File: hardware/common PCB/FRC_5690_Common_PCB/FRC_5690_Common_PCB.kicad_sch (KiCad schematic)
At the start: 33 parts, among them J1 5V in, J10 UART, J11 LED 0, J12 LED 1, J13 Analog In, J17 Conn_01x03_Pin, J18 Conn_01x03_Pin, J19 Conn_01x03_Pin, J2 I2C 0, J20 Conn_01x03_Pin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

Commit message: migrate to Pico code and add micro SD card slot
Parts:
- added C3: 100nF, Capacitor_SMD:C_0603_1608Metric, symbol Device:C
- added J14: Micro_SD_Card, Connector_Card:microSD_HC_Hirose_DM3BT-DSF-PEJS, symbol Connector:Micro_SD_Card
- added R5: 1k, Resistor_SMD:R_0603_1608Metric, symbol Device:R
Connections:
- net +3.3V: now also C3.1, J14.4 (VDD), R5.1
- net GND: now also C3.2, J14.6 (VSS), J14.9 (SHIELD)
- net SPI1_CLK: now also J14.5 (CLK)
- net SPI1_MISO: now also J14.7 (DAT0)
- net SPI1_MOSI: now also J14.3 (CMD)
- net SD_CARD_CS: now reaches U1.29 (GPIO22)
- net SD_CARD_CS: now also J14.2 (DAT3/CD), R5.2
- no-connect marks 0 -> 2

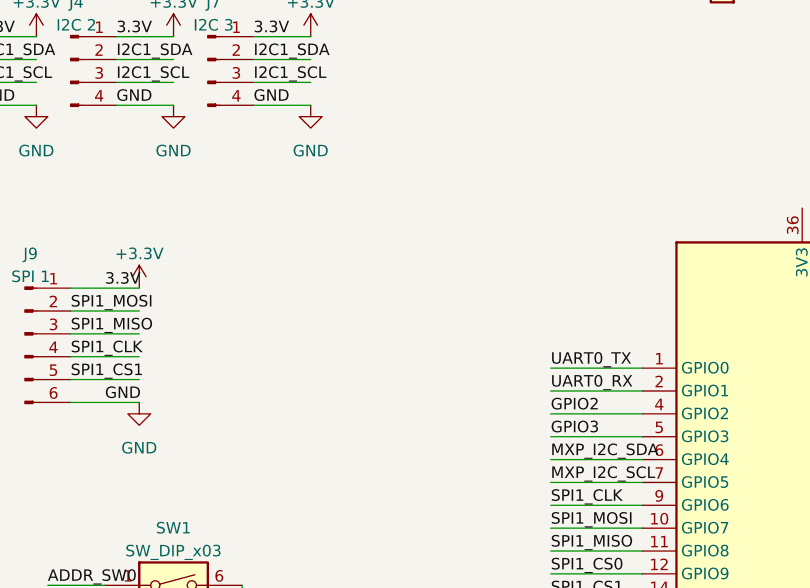
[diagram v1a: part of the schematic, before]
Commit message: Add EEPROM
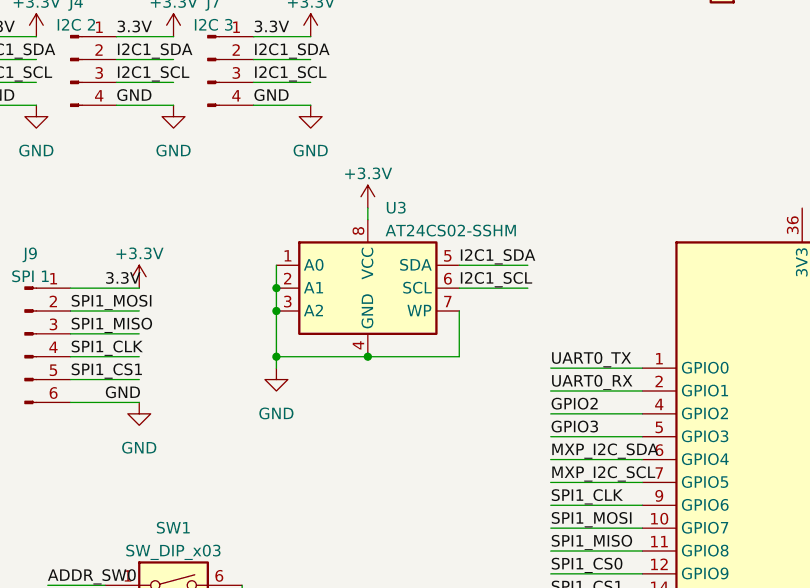
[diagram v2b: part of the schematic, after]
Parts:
- added U3: AT24CS02-SSHM, Package_SO:SOIC-8_3.9x4.9mm_P1.27mm, symbol Memory_EEPROM:AT24CS02-SSHM
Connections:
- net +3.3V: now also U3.8 (VCC)
- net GND: now also U3.1 (A0), U3.2 (A1), U3.3 (A2), U3.4 (GND), U3.7 (WP)
- net I2C1_SCL: now also U3.6 (SCL)
- net I2C1_SDA: now also U3.5 (SDA)
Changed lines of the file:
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@@
     (comment 1 "Designed by Evan Rust")
   )
+  (junction (at 88.9 73.66) (diameter 0) (color 0 0 0 0)
+  )
   (junction (at 222.25 149.86) (diameter 0) (color 0 0 0 0)
   )
@@
   (junction (at 232.41 49.53) (diameter 0) (color 0 0 0 0)
   )
+  (junction (at 99.06 73.66) (diameter 0) (color 0 0 0 0)
+  )
+  (junction (at 88.9 66.04) (diameter 0) (color 0 0 0 0)
+  )
   (junction (at 222.25 133.35) (diameter 0) (color 0 0 0 0)
   )
   (junction (at 232.41 93.98) (diameter 0) (color 0 0 0 0)
   )
+  (junction (at 88.9 68.58) (diameter 0) (color 0 0 0 0)
+  )
   (junction (at 224.79 63.5) (diameter 0) (color 0 0 0 0)
   )
@@
     (stroke (width 0) (type default))
   )
+  (wire (pts (xy 109.22 68.58) (xy 109.22 73.66))
+    (stroke (width 0) (type default))
+  )
   (wire (pts (xy 36.83 152.4) (xy 46.99 152.4))
     (stroke (width 0) (type default))
@@
     (stroke (width 0) (type default))
   )
+  (wire (pts (xy 99.06 57.15) (xy 99.06 58.42))
+    (stroke (width 0) (type default))
+  )
   (wire (pts (xy 116.84 182.88) (xy 125.73 182.88))
     (stroke (width 0) (type default))
@@
     (stroke (width 0) (type default))
   )
+  (wire (pts (xy 99.06 73.66) (xy 88.9 73.66))
+    (stroke (width 0) (type default))
+  )
+  (wire (pts (xy 88.9 66.04) (xy 88.9 68.58))
+    (stroke (width 0) (type default))
+  )
   (wire (pts (xy 119.38 102.87) (xy 129.54 102.87))
     (stroke (width 0) (type default))
@@
     (stroke (width 0) (type default))
   )
+  (wire (pts (xy 88.9 68.58) (xy 88.9 73.66))
+    (stroke (width 0) (type default))
+  )
   (wire (pts (xy 189.23 146.05) (xy 194.31 146.05))
     (stroke (width 0) (type default))
@@
     (stroke (width 0) (type default))
   )
+  (wire (pts (xy 99.06 73.66) (xy 109.22 73.66))
+    (stroke (width 0) (type default))
+  )
   (wire (pts (xy 232.41 118.11) (xy 232.41 119.38))
     (stroke (width 0) (type default))
@@
     (stroke (width 0) (type default))
   )
+  (wire (pts (xy 88.9 73.66) (xy 88.9 74.93))
+    (stroke (width 0) (type default))
+  )
   (wire (pts (xy 119.38 90.17) (xy 129.54 90.17))
     (stroke (width 0) (type default))
@@
     (stroke (width 0) (type default))
   )
+  (wire (pts (xy 88.9 63.5) (xy 88.9 66.04))
+    (stroke (width 0) (type default))
+  )
   (wire (pts (xy 91.44 144.78) (xy 104.14 144.78))
     (stroke (width 0) (type default))
@@
     (stroke (width 0) (type default))
   )
+  (wire (pts (xy 109.22 63.5) (xy 116.84 63.5))
+    (stroke (width 0) (type default))
+  )
   (wire (pts (xy 119.38 85.09) (xy 129.54 85.09))
     (stroke (width 0) (type default))
   )
+  (wire (pts (xy 109.22 66.04) (xy 116.84 66.04))
+    (stroke (width 0) (type default))
+  )
   (wire (pts (xy 66.04 76.2) (xy 73.66 76.2))
     (stroke (width 0) (type default))
@@
     (effects (font (size 1.27 1.27)) (justify left bottom))
   )
+  (label "I2C1_SDA" (at 109.22 63.5 0) (fields_autoplaced)
+    (effects (font (size 1.27 1.27)) (justify left bottom))
+  )
   (label "SPI1_MISO" (at 41.91 71.12 0) (fields_autoplaced)
     (effects (font (size 1.27 1.27)) (justify left bottom))
@@
     (effects (font (size 1.27 1.27)) (justify left bottom))
   )
+  (label "I2C1_SCL" (at 109.22 66.04 0) (fields_autoplaced)
+    (effects (font (size 1.27 1.27)) (justify left bottom))
+  )
   (label "GPIO3" (at 189.23 135.89 0) (fields_autoplaced)
     (effects (font (size 1.27 1.27)) (justify left bottom))
@@
     )
   )
+  (symbol (lib_id "power:GND") (at 88.9 74.93 0) (unit 1)
+    (in_bom yes) (on_board yes) (dnp no) (fields_autoplaced)
+    (property "Reference" "#PWR060" (at 88.9 81.28 0)
+      (effects (font (size 1.27 1.27)) hide)
+    )
+    (property "Value" "GND" (at 88.9 80.01 0)
+      (effects (font (size 1.27 1.27)))
+    )
+    (property "Footprint" "" (at 88.9 74.93 0)
+      (effects (font (size 1.27 1.27)) hide)
+    )
+    (property "Datasheet" "" (at 88.9 74.93 0)
+      (effects (font (size 1.27 1.27)) hide)
+    )
+    (pin "1")
+    (instances
+      (project "FRC_5690_Common_PCB"
+        (path "/61912a13-ede8-48b1-a32d-9390036060d9"
+          (reference "#PWR060") (unit 1)
+        )
+      )
+    )
+  )
   (symbol (lib_id "Transistor_BJT:BC849W") (at 215.9 113.03 0) (unit 1)
     (in_bom yes) (on_board yes) (dnp no) (fields_autoplaced)
@@
     )
   )
+  (symbol (lib_id "power:+3.3V") (at 99.06 57.15 0) (unit 1)
+    (in_bom yes) (on_board yes) (dnp no) (fields_autoplaced)
+    (property "Reference" "#PWR059" (at 99.06 60.96 0)
+      (effects (font (size 1.27 1.27)) hide)
+    )
+    (property "Value" "+3.3V" (at 99.06 53.34 0)
+      (effects (font (size 1.27 1.27)))
+    )
+    (property "Footprint" "" (at 99.06 57.15 0)
+      (effects (font (size 1.27 1.27)) hide)
+    )
+    (property "Datasheet" "" (at 99.06 57.15 0)
+      (effects (font (size 1.27 1.27)) hide)
+    )
+    (pin "1")
+    (instances
+      (project "FRC_5690_Common_PCB"
+        (path "/61912a13-ede8-48b1-a32d-9390036060d9"
+          (reference "#PWR059") (unit 1)
+        )
+      )
+    )
+  )
   (symbol (lib_id "Connector:Screw_Terminal_01x02") (at 138.43 33.02 180) (unit 1)
     (in_bom yes) (on_board yes) (dnp no) (fields_autoplaced)
@@
         )
       )
+    )
+  )
+  (symbol (lib_id "Memory_EEPROM:AT24CS02-SSHM") (at 99.06 66.04 0) (unit 1)
+    (in_bom yes) (on_board yes) (dnp no) (fields_autoplaced)
+    (property "Reference" "U3" (at 101.0159 57.15 0)
+      (effects (font (size 1.27 1.27)) (justify left))
+    )
+    (property "Value" "AT24CS02-SSHM" (at 101.0159 59.69 0)
+      (effects (font (size 1.27 1.27)) (justify left))
+    )
+    (property "Footprint" "Package_SO:SOIC-8_3.9x4.9mm_P1.27mm" (at 99.06 66.04 0)
+      (effects (font (size 1.27 1.27)) hide)
+    )
+    (property "Datasheet" "http://ww1.microchip.com/downloads/en/DeviceDoc/Atmel-8815-SEEPROM-AT24CS01-02-Datasheet.pdf" (at 99.06 66.04 0)
+      (effects (font (size 1.27 1.27)) hide)
+    )
+    (pin "1")
+    (pin "2")
+    (pin "3")
+    (pin "4")
+    (pin "5")
+    (pin "6")
+    (pin "7")
+    (pin "8")
+    (instances
+      (project "FRC_5690_Common_PCB"
+        (path "/61912a13-ede8-48b1-a32d-9390036060d9"
+          (reference "U3") (unit 1)
+        )
+      )

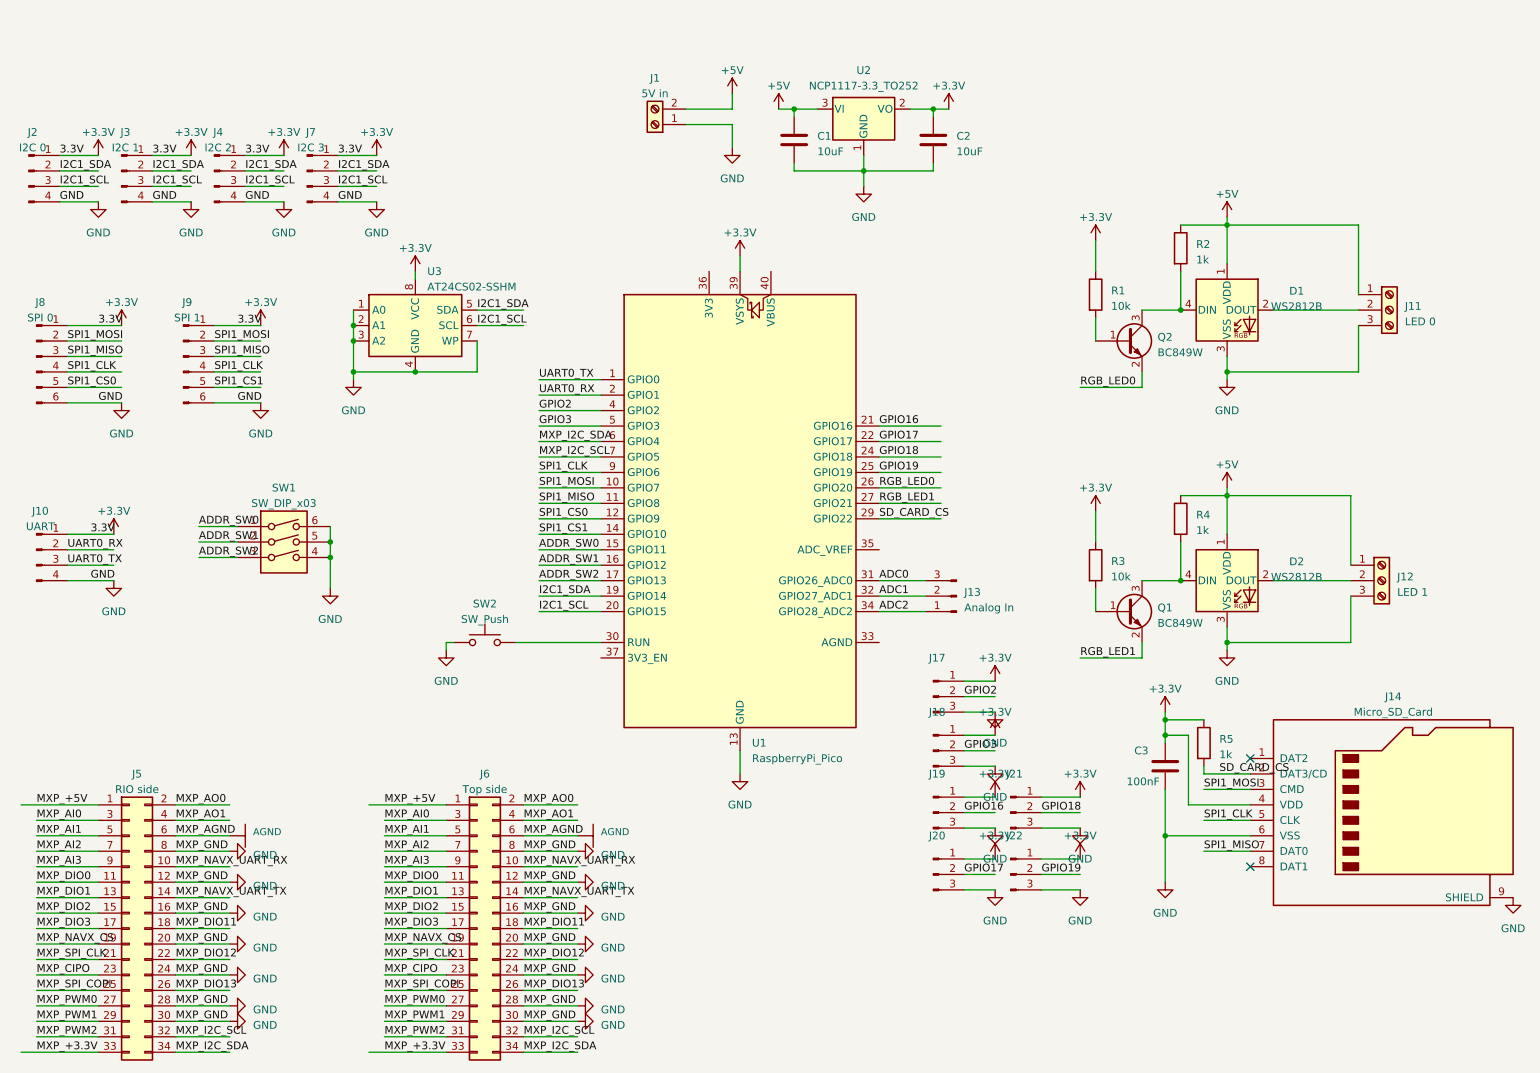
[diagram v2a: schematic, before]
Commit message: add configuration for eeprom
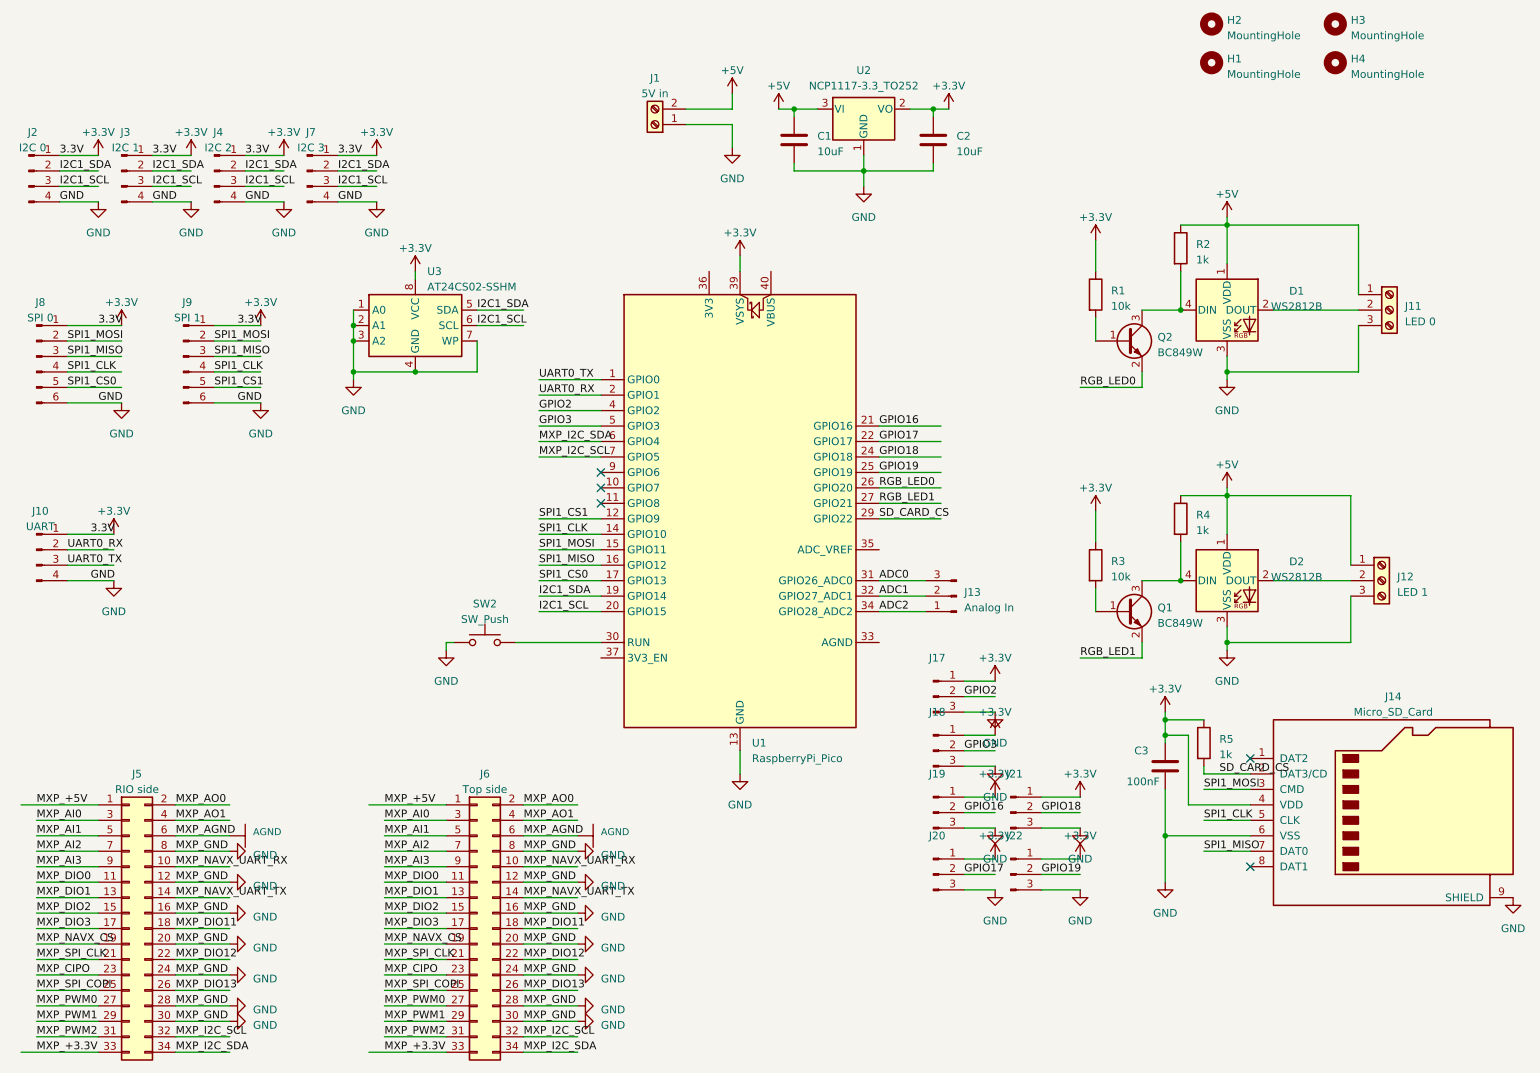
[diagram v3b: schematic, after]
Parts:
- removed SW1: SW_DIP_x03, Button_Switch_SMD:SW_DIP_SPSTx03_Slide_6.7x9.18mm_W8.61mm_P2.54mm_LowProfile, symbol Switch:SW_DIP_x03
- added H1, H2, H3, H4: MountingHole, MountingHole:MountingHole_3.2mm_M3_DIN965_Pad, symbol Mechanical:MountingHole
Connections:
- net ADDR_SW0 is gone; now on net SPI1_MOSI: U1.15 (GPIO11)
- net ADDR_SW1 is gone; now on net SPI1_MISO: U1.16 (GPIO12)
- net ADDR_SW2 is gone; now on net SPI1_CS0: U1.17 (GPIO13)
- net SPI1_CLK: now also U1.14 (GPIO10); no longer U1.9 (GPIO6)
- net SPI1_CS0: no longer U1.12 (GPIO9)
- net SPI1_CS1: now also U1.12 (GPIO9); no longer U1.14 (GPIO10)
- net SPI1_MISO: no longer U1.11 (GPIO8)
- net SPI1_MOSI: no longer U1.10 (GPIO7)
- no-connect marks 2 -> 5
